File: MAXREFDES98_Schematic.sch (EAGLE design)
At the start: 34 parts, among them U1 MB110S-TP, U2 MB110S-TP, U3 MAX5969AETB+

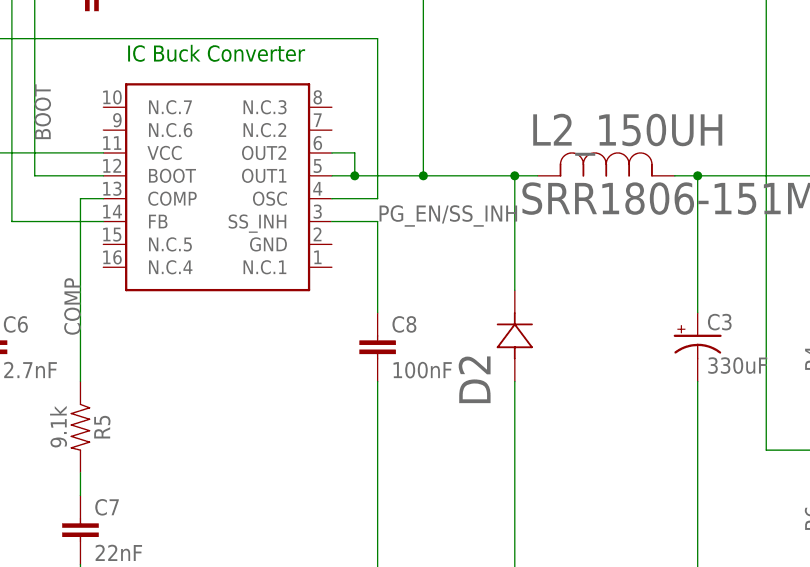
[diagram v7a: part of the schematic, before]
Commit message: Added GND to Buck and changed some wire widths.
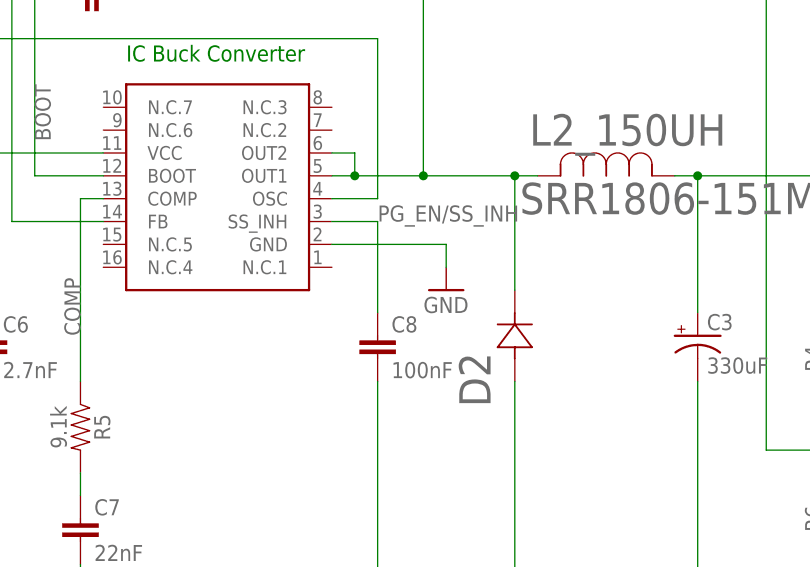
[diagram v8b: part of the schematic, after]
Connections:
- net GND: now also U$1.GND
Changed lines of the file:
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@@
 <part name="C3" library="CameraBoard_Library" deviceset="337AXZ025M" device=""/>
 <part name="FRAME2" library="SparkFun-Aesthetics" library_urn="urn:adsk.eagle:library:507" deviceset="FRAME-A4L" device=""/>
+<part name="GND5" library="supply1" library_urn="urn:adsk.eagle:library:371" deviceset="GND" device=""/>
 </parts>
 <sheets>
@@
 <attribute name="LAST_DATE_TIME" x="181.61" y="6.35" size="2.286" layer="94" font="vector"/>
 <attribute name="SHEET" x="195.58" y="1.27" size="2.54" layer="94" font="vector"/>
+</instance>
+<instance part="GND5" gate="1" x="208.28" y="71.12" smashed="yes">
+<attribute name="VALUE" x="205.74" y="68.58" size="1.778" layer="96"/>
 </instance>
 </instances>
@@
 <pinref part="GND4" gate="1" pin="GND"/>
 </segment>
-</net>
+<segment>
+<pinref part="U$1" gate="G$1" pin="GND"/>
+<wire x1="195.58" y1="76.2" x2="208.28" y2="76.2" width="0.1524" layer="91"/>
+<wire x1="208.28" y1="76.2" x2="208.28" y2="73.66" width="0.1524" layer="91"/>
+<pinref part="GND5" gate="1" pin="GND"/>
+</segment>
+</net>
